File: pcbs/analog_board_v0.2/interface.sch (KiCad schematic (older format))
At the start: 2 parts

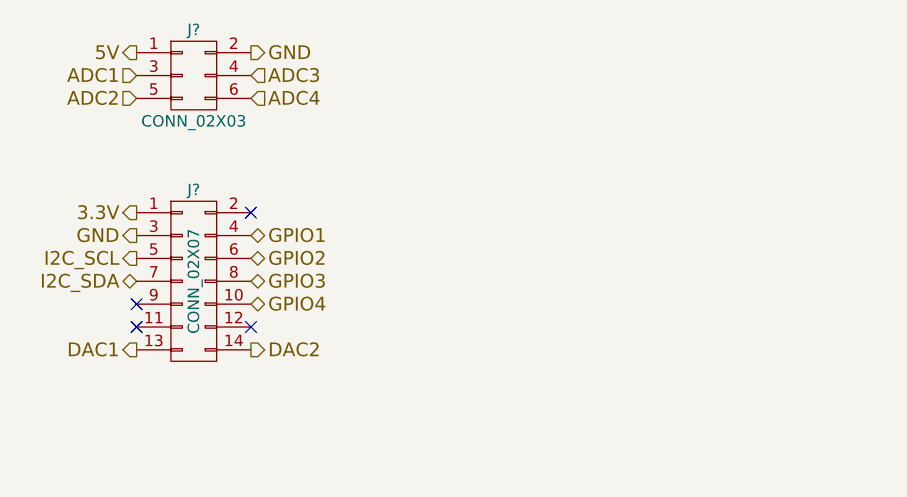
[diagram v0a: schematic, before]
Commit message: Finished schematics of the analog_board_v0.2 today.
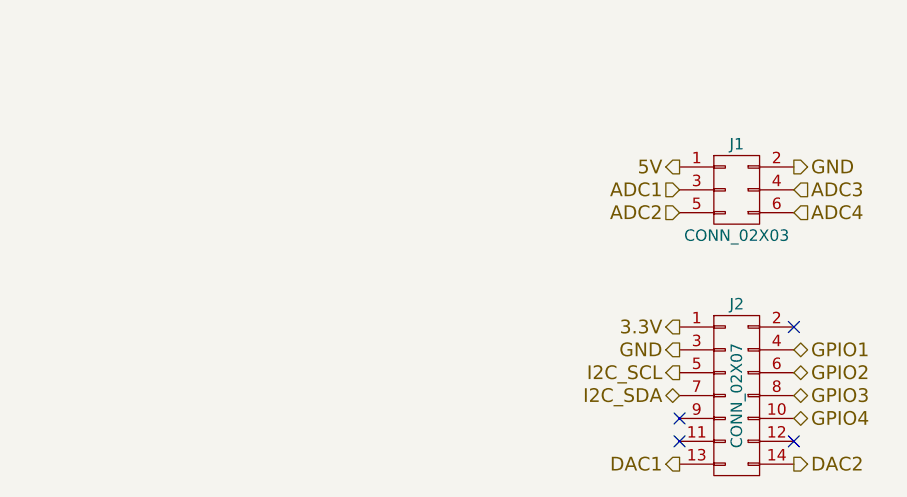
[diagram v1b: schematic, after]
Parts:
- gave numbers to parts that had none: 2
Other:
- moved on the sheet: J1, J2
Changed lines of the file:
@@
 LIBS:ad8616
 LIBS:icl7660
-LIBS:analog_board-cache
+LIBS:ada4530-1
+LIBS:ada4522-2
 EELAYER 25 0
 EELAYER END
@@
 Sheet 3 4
 Title "Interface to Backplane"
-Date "2017-06-29"
+Date "2017-06-30"
 Rev ""
-Comp ""
+Comp "UppSense"
 Comment1 ""
 Comment2 ""
@@
 $EndDescr
 $Comp
-L CONN_02X03 J?
+L CONN_02X03 J1
 U 1 1 5954E6D0
-P 3750 2500
-F 0 "J?" H 3750 2700 50  0000 C CNN
-F 1 "CONN_02X03" H 3750 2300 50  0000 C CNN
-F 2 "" H 3750 1300 50  0001 C CNN
-F 3 "" H 3750 1300 50  0001 C CNN
-	1    3750 2500
+P 6125 3000
+F 0 "J1" H 6125 3200 50  0000 C CNN
+F 1 "CONN_02X03" H 6125 2800 50  0000 C CNN
+F 2 "" H 6125 1800 50  0001 C CNN
+F 3 "" H 6125 1800 50  0001 C CNN
+	1    6125 3000
 	1    0    0    -1
 $EndComp
-Text HLabel 3500 2400 0    60   Output ~ 0
+Text HLabel 5875 2900 0    60   Output ~ 0
 5V
-Text HLabel 3500 2500 0    60   Input ~ 0
+Text HLabel 5875 3000 0    60   Input ~ 0
 ADC1
-Text HLabel 3500 2600 0    60   Input ~ 0
+Text HLabel 5875 3100 0    60   Input ~ 0
 ADC2
-Text HLabel 4000 2500 2    60   Input ~ 0
+Text HLabel 6375 3000 2    60   Input ~ 0
 ADC3
-Text HLabel 4000 2600 2    60   Input ~ 0
+Text HLabel 6375 3100 2    60   Input ~ 0
 ADC4
-Text HLabel 4000 2400 2    60   Output ~ 0
+Text HLabel 6375 2900 2    60   Output ~ 0
 GND
 $Comp
-L CONN_02X07 J?
+L CONN_02X07 J2
 U 1 1 5954E8F2
-P 3750 3400
-F 0 "J?" H 3750 3800 50  0000 C CNN
-F 1 "CONN_02X07" V 3750 3400 50  0000 C CNN
-F 2 "" H 3750 2200 50  0001 C CNN
-F 3 "" H 3750 2200 50  0001 C CNN
-	1    3750 3400
+P 6125 3900
+F 0 "J2" H 6125 4300 50  0000 C CNN
+F 1 "CONN_02X07" V 6125 3900 50  0000 C CNN
+F 2 "" H 6125 2700 50  0001 C CNN
+F 3 "" H 6125 2700 50  0001 C CNN
+	1    6125 3900
 	1    0    0    -1
 $EndComp
-Text HLabel 3500 3100 0    60   Output ~ 0
+Text HLabel 5875 3600 0    60   Output ~ 0
 3.3V
-Text HLabel 3500 3200 0    60   Output ~ 0
+Text HLabel 5875 3700 0    60   Output ~ 0
 GND
-Text HLabel 3500 3300 0    60   Output ~ 0
+Text HLabel 5875 3800 0    60   Output ~ 0
 I2C_SCL
-Text HLabel 3500 3400 0    60   BiDi ~ 0
+Text HLabel 5875 3900 0    60   BiDi ~ 0
 I2C_SDA
-Text HLabel 3500 3700 0    60   Output ~ 0
+Text HLabel 5875 4200 0    60   Output ~ 0
 DAC1
-Text HLabel 4000 3700 2    60   Output ~ 0
+Text HLabel 6375 4200 2    60   Output ~ 0
 DAC2
-NoConn ~ 3500 3600
-NoConn ~ 3500 3500
-NoConn ~ 4000 3600
-Text HLabel 4000 3500 2    60   BiDi ~ 0
+NoConn ~ 5875 4100
+NoConn ~ 5875 4000
+NoConn ~ 6375 4100
+Text HLabel 6375 4000 2    60   BiDi ~ 0
 GPIO4
-Text HLabel 4000 3400 2    60   BiDi ~ 0
+Text HLabel 6375 3900 2    60   BiDi ~ 0
 GPIO3
-Text HLabel 4000 3300 2    60   BiDi ~ 0
+Text HLabel 6375 3800 2    60   BiDi ~ 0
 GPIO2
-Text HLabel 4000 3200 2    60   BiDi ~ 0
+Text HLabel 6375 3700 2    60   BiDi ~ 0
 GPIO1
-NoConn ~ 4000 3100
+NoConn ~ 6375 3600
 $EndSCHEMATC

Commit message: Added some iportant backplane spec.
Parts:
- J1: footprint (none) -> Pin_Headers:Pin_Header_Angled_2x03_Pitch2.54mm
- J2: footprint (none) -> Pin_Headers:Pin_Header_Angled_2x07_Pitch2.54mm
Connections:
- net 3.3V: now also J2.13 (P13); no longer J2.1 (P1)
- net 5V: now also J1.2 (P2); no longer J1.1 (P1)
- net ADC1: now also J1.4 (P4); no longer J1.3 (P3)
- net ADC2: now also J1.6 (P6); no longer J1.5 (P5)
- net ADC3: now also J1.3 (P3); no longer J1.4 (P4)
- net ADC4: now also J1.5 (P5); no longer J1.6 (P6)
- net DAC1: now also J2.1 (P1); no longer J2.13 (P13)
- net DAC2: now also J2.2 (P2); no longer J2.14 (P14)
- net GND: now also J1.1 (P1), J2.11 (P11); no longer J1.2 (P2), J2.3 (P3)
- net GPIO1: now also J2.12 (P12); no longer J2.4 (P4)
- net GPIO2: now also J2.10 (P10); no longer J2.6 (P6)
- net GPIO4: now also J2.6 (P6); no longer J2.10 (P10)
- net I2C_SCL: now also J2.9 (P9); no longer J2.5 (P5)
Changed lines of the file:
@@
 LIBS:ada4530-1
 LIBS:ada4522-2
+LIBS:analog_board_v0.2-cache
 EELAYER 25 0
 EELAYER END
@@
 F 0 "J1" H 6125 3200 50  0000 C CNN
 F 1 "CONN_02X03" H 6125 2800 50  0000 C CNN
-F 2 "" H 6125 1800 50  0001 C CNN
+F 2 "Pin_Headers:Pin_Header_Angled_2x03_Pitch2.54mm" H 6125 1800 50  0001 C CNN
 F 3 "" H 6125 1800 50  0001 C CNN
 	1    6125 3000
 	1    0    0    -1
 $EndComp
+Text HLabel 6375 2900 2    60   Output ~ 0
+5V
+Text HLabel 6375 3000 2    60   Input ~ 0
+ADC1
+Text HLabel 6375 3100 2    60   Input ~ 0
+ADC2
+Text HLabel 5875 3000 0    60   Input ~ 0
+ADC3
+Text HLabel 5875 3100 0    60   Input ~ 0
+ADC4
 Text HLabel 5875 2900 0    60   Output ~ 0
-5V
-Text HLabel 5875 3000 0    60   Input ~ 0
-ADC1
-Text HLabel 5875 3100 0    60   Input ~ 0
-ADC2
-Text HLabel 6375 3000 2    60   Input ~ 0
-ADC3
-Text HLabel 6375 3100 2    60   Input ~ 0
-ADC4
-Text HLabel 6375 2900 2    60   Output ~ 0
 GND
 $Comp
@@
 F 0 "J2" H 6125 4300 50  0000 C CNN
 F 1 "CONN_02X07" V 6125 3900 50  0000 C CNN
-F 2 "" H 6125 2700 50  0001 C CNN
+F 2 "Pin_Headers:Pin_Header_Angled_2x07_Pitch2.54mm" H 6125 2700 50  0001 C CNN
 F 3 "" H 6125 2700 50  0001 C CNN
 	1    6125 3900
 	1    0    0    -1
 $EndComp
-Text HLabel 5875 3600 0    60   Output ~ 0
+Text HLabel 5875 4200 0    60   Output ~ 0
 3.3V
-Text HLabel 5875 3700 0    60   Output ~ 0
+Text HLabel 5875 4100 0    60   Output ~ 0
 GND
-Text HLabel 5875 3800 0    60   Output ~ 0
+Text HLabel 5875 4000 0    60   Output ~ 0
 I2C_SCL
 Text HLabel 5875 3900 0    60   BiDi ~ 0
 I2C_SDA
-Text HLabel 5875 4200 0    60   Output ~ 0
+Text HLabel 5875 3600 0    60   Output ~ 0
 DAC1
-Text HLabel 6375 4200 2    60   Output ~ 0
+Text HLabel 6375 3600 2    60   Output ~ 0
 DAC2
-NoConn ~ 5875 4100
-NoConn ~ 5875 4000
-NoConn ~ 6375 4100
-Text HLabel 6375 4000 2    60   BiDi ~ 0
+NoConn ~ 5875 3700
+NoConn ~ 5875 3800
+NoConn ~ 6375 3700
+Text HLabel 6375 3800 2    60   BiDi ~ 0
 GPIO4
 Text HLabel 6375 3900 2    60   BiDi ~ 0
 GPIO3
-Text HLabel 6375 3800 2    60   BiDi ~ 0
+Text HLabel 6375 4000 2    60   BiDi ~ 0
 GPIO2
-Text HLabel 6375 3700 2    60   BiDi ~ 0
+Text HLabel 6375 4100 2    60   BiDi ~ 0
 GPIO1
-NoConn ~ 6375 3600
+NoConn ~ 6375 4200
 $EndSCHEMATC

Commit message: Backplane definitely finished. Somethings wrong with TIA. Has to be checked tomorrow.
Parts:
- J1: Samtec (none) -> TSW-103-08-G-D-RA
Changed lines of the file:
@@
 F 1 "CONN_02X03" H 6125 2800 50  0000 C CNN
 F 2 "Pin_Headers:Pin_Header_Angled_2x03_Pitch2.54mm" H 6125 1800 50  0001 C CNN
-F 3 "" H 6125 1800 50  0001 C CNN
+F 3 "http://suddendocs.samtec.com/catalog_english/tsw_th.pdf" H 6125 1800 50  0001 C CNN
+F 4 "TSW-103-08-G-D-RA" H 6125 3000 60  0001 C CNN "Samtec"
 	1    6125 3000
 	1    0    0    -1

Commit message: Added BOMs and gerber files.
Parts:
- J2: Samtec (none) -> TSW-107-08-G-D-RA
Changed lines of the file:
@@
 F 2 "Pin_Headers:Pin_Header_Angled_2x07_Pitch2.54mm" H 6125 2700 50  0001 C CNN
 F 3 "" H 6125 2700 50  0001 C CNN
+F 4 "TSW-107-08-G-D-RA" H 6125 3900 60  0001 C CNN "Samtec"
 	1    6125 3900
 	1    0    0    -1
